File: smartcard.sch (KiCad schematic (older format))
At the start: 9 parts, among them J2101 Smart_Card, U2101 SEC1110

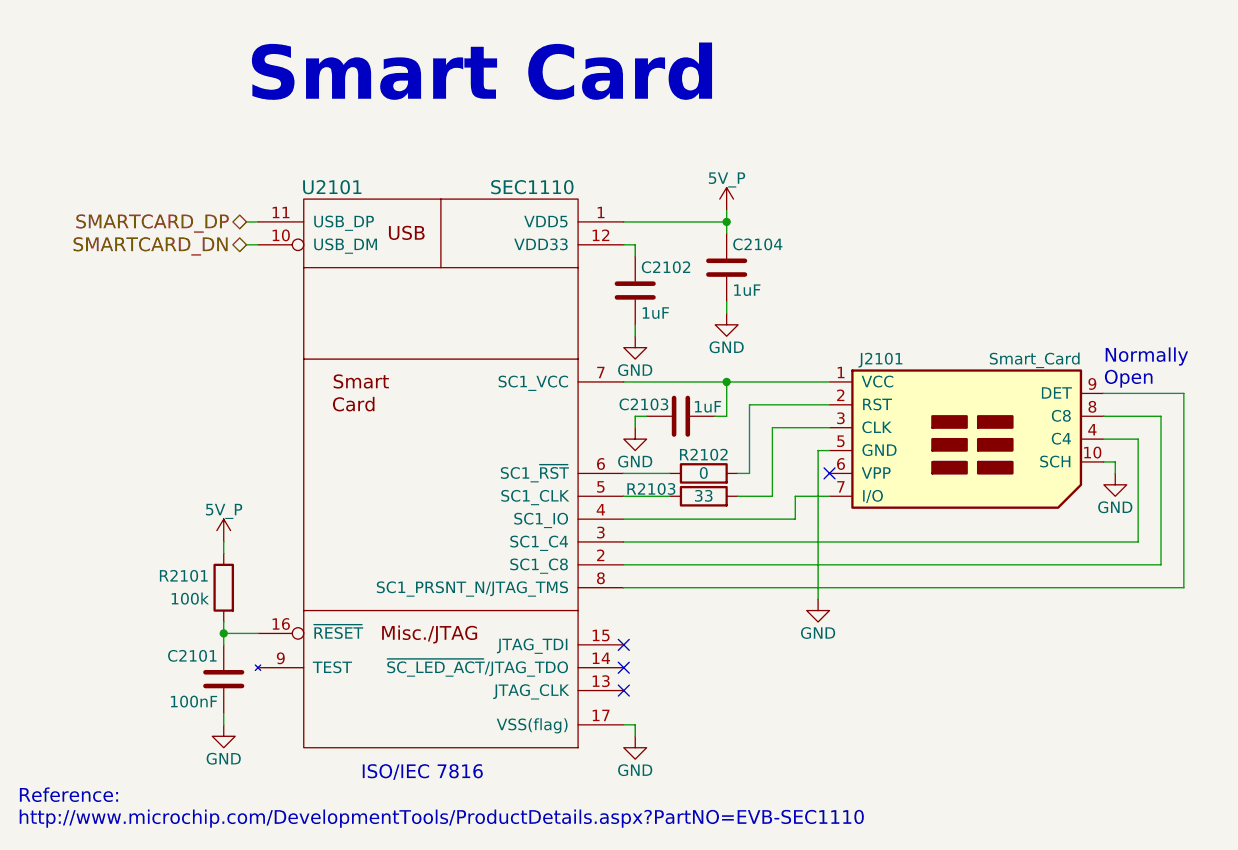
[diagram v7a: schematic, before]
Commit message: Move the WLAN+BT M.2 sheet back to page 18 rather than the last page (24)
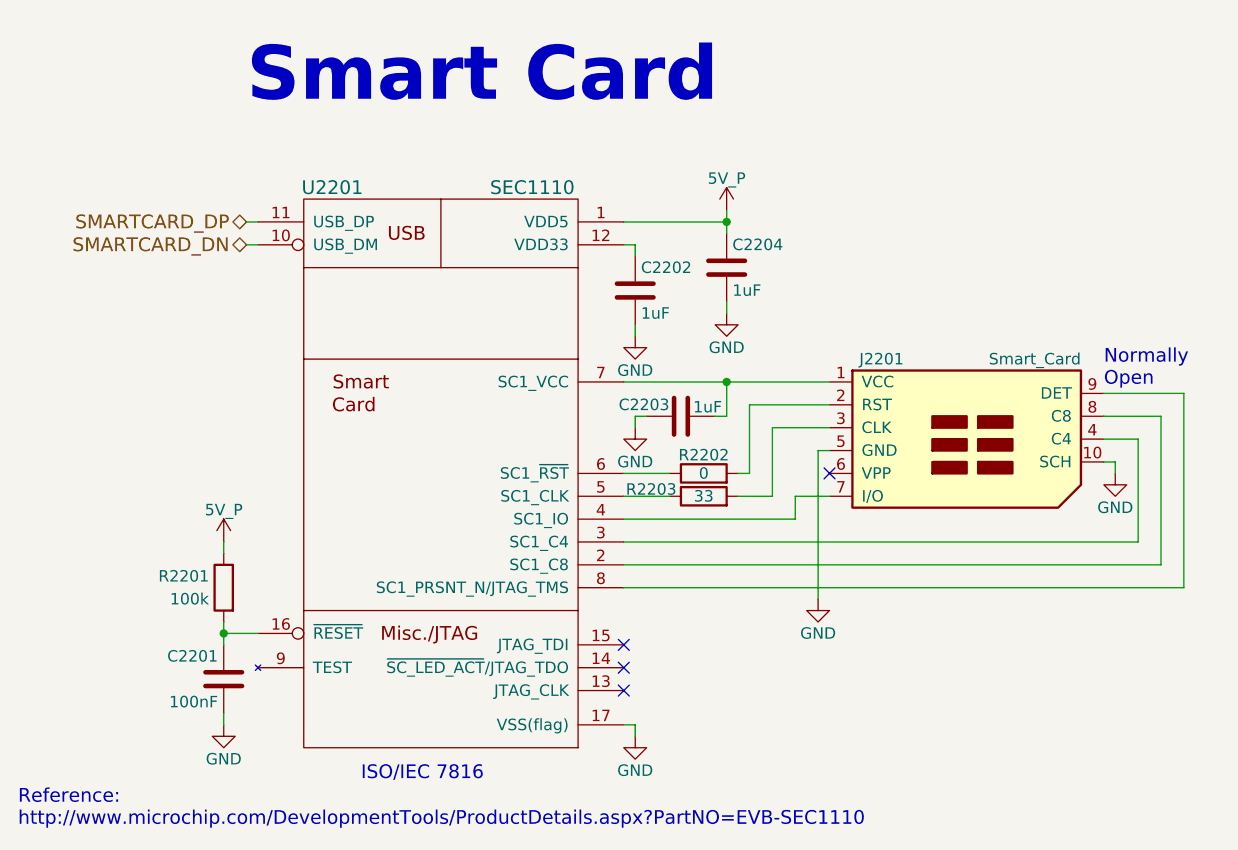
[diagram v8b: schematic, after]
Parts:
- renumbered C2101 to C2201, C2102 to C2202, C2103 to C2203, C2104 to C2204, J2101 to J2201, R2101 to R2201, R2102 to R2202, R2103 to R2203, U2101 to U2201
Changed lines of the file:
@@
 $Descr A4 11693 8268
 encoding utf-8
-Sheet 21 24
+Sheet 22 24
 Title "Smart Card"
-Date "2018-06-14"
+Date "2018-06-15"
 Rev "v0.1.0"
 Comp "Copyright 2018 GNU GPLv3"
@@
 SMARTCARD_DN
 $Comp
-L 5V_P #PWR0333
+L 5V_P #PWR0359
 U 1 1 5B1F0A54
 P 6900 2250
-F 0 "#PWR0333" H 6900 2100 50  0001 C CNN
+F 0 "#PWR0359" H 6900 2100 50  0001 C CNN
 F 1 "5V_P" H 6900 2390 50  0000 C CNN
 F 2 "" H 6900 2250 50  0001 C CNN
@@
 $EndComp
 $Comp
-L C C2102
+L C C2202
 U 1 1 5B1F1971
 P 6500 2600
-F 0 "C2102" H 6525 2700 50  0000 L CNN
+F 0 "C2202" H 6525 2700 50  0000 L CNN
 F 1 "1uF" H 6525 2500 50  0000 L CNN
 F 2 "Capacitors_SMD:C_0603" H 6538 2450 50  0001 C CNN
@@
 $EndComp
 $Comp
-L GND #PWR0334
+L GND #PWR0360
 U 1 1 5B1F199A
 P 6500 2800
-F 0 "#PWR0334" H 6500 2550 50  0001 C CNN
+F 0 "#PWR0360" H 6500 2550 50  0001 C CNN
 F 1 "GND" H 6500 2650 50  0000 C CNN
 F 2 "" H 6500 2800 50  0001 C CNN
@@
 $EndComp
 $Comp
-L C C2104
+L C C2204
 U 1 1 5B1F1CFA
 P 6900 2500
-F 0 "C2104" H 6925 2600 50  0000 L CNN
+F 0 "C2204" H 6925 2600 50  0000 L CNN
 F 1 "1uF" H 6925 2400 50  0000 L CNN
 F 2 "Capacitors_SMD:C_0603" H 6938 2350 50  0001 C CNN
@@
 $EndComp
 $Comp
-L GND #PWR0335
+L GND #PWR0361
 U 1 1 5B1F1D4E
 P 6900 2700
-F 0 "#PWR0335" H 6900 2450 50  0001 C CNN
+F 0 "#PWR0361" H 6900 2450 50  0001 C CNN
 F 1 "GND" H 6900 2550 50  0000 C CNN
 F 2 "" H 6900 2700 50  0001 C CNN
@@
 $EndComp
 $Comp
-L R R2102
+L R R2202
 U 1 1 5B1F2A2C
 P 6800 3400
-F 0 "R2102" V 6880 3400 50  0000 C CNN
+F 0 "R2202" V 6880 3400 50  0000 C CNN
 F 1 "0" V 6800 3400 50  0000 C CNN
 F 2 "Resistors_SMD:R_0603" V 6730 3400 50  0001 C CNN
@@
 $EndComp
 $Comp
-L R R2103
+L R R2203
 U 1 1 5B1F2AD0
 P 6800 3500
-F 0 "R2103" V 6830 3730 50  0000 C CNN
+F 0 "R2203" V 6830 3730 50  0000 C CNN
 F 1 "33" V 6800 3500 50  0000 C CNN
 F 2 "Resistors_SMD:R_0603" V 6730 3500 50  0001 C CNN
@@
 NoConn ~ 6450 4350
 $Comp
-L R R2101
+L R R2201
 U 1 1 5B20FE9D
 P 4700 3900
-F 0 "R2101" H 4875 3950 50  0000 C CNN
+F 0 "R2201" H 4875 3950 50  0000 C CNN
 F 1 "100k" H 4850 3850 50  0000 C CNN
 F 2 "Resistors_SMD:R_0603" V 4630 3900 50  0001 C CNN
@@
 $EndComp
 $Comp
-L 5V_P #PWR0336
+L 5V_P #PWR0362
 U 1 1 5B20FF3B
 P 4700 3700
-F 0 "#PWR0336" H 4700 3550 50  0001 C CNN
+F 0 "#PWR0362" H 4700 3550 50  0001 C CNN
 F 1 "5V_P" H 4700 3840 50  0000 C CNN
 F 2 "" H 4700 3700 50  0001 C CNN
@@
 $EndComp
 $Comp
-L C C2101
+L C C2201
 U 1 1 5B20FF65
 P 4700 4300
-F 0 "C2101" H 4725 4400 50  0000 L CNN
+F 0 "C2201" H 4725 4400 50  0000 L CNN
 F 1 "100nF" H 4725 4200 50  0000 L CNN
 F 2 "Capacitors_SMD:C_0603" H 4738 4150 50  0001 C CNN
@@
 $EndComp
 $Comp
-L GND #PWR0337
+L GND #PWR0363
 U 1 1 5B20FFAF
 P 4700 4500
-F 0 "#PWR0337" H 4700 4250 50  0001 C CNN
+F 0 "#PWR0363" H 4700 4250 50  0001 C CNN
 F 1 "GND" H 4700 4350 50  0000 C CNN
 F 2 "" H 4700 4500 50  0001 C CNN
@@
 $EndComp
 $Comp
-L C C2103
+L C C2203
 U 1 1 5B210DE6
 P 6700 3150
-F 0 "C2103" V 6750 3200 50  0000 L CNN
+F 0 "C2203" V 6750 3200 50  0000 L CNN
 F 1 "1uF" V 6740 2970 50  0000 L CNN
 F 2 "Capacitors_SMD:C_0603" H 6738 3000 50  0001 C CNN
@@
 $EndComp
 $Comp
-L GND #PWR0338
+L GND #PWR0364
 U 1 1 5B210E33
 P 6500 3200
-F 0 "#PWR0338" H 6500 2950 50  0001 C CNN
+F 0 "#PWR0364" H 6500 2950 50  0001 C CNN
 F 1 "GND" H 6500 3050 50  0000 C CNN
 F 2 "" H 6500 3200 50  0001 C CNN
@@
 $EndComp
 $Comp
-L GND #PWR0339
+L GND #PWR0365
 U 1 1 5B21589D
 P 6500 4550
-F 0 "#PWR0339" H 6500 4300 50  0001 C CNN
+F 0 "#PWR0365" H 6500 4300 50  0001 C CNN
 F 1 "GND" H 6500 4400 50  0000 C CNN
 F 2 "" H 6500 4550 50  0001 C CNN
@@
 ISO/IEC 7816
 $Comp
-L SEC1110 U2101
+L SEC1110 U2201
 U 1 1 5B265531
 P 5650 3400
-F 0 "U2101" H 5175 4650 60  0000 C CNN
+F 0 "U2201" H 5175 4650 60  0000 C CNN
 F 1 "SEC1110" H 6050 4650 60  0000 C CNN
 F 2 "" H 5650 3700 60  0001 C CNN
@@
 $EndComp
 $Comp
-L SMART_CARD J2101
+L SMART_CARD J2201
 U 1 1 5B26711A
 P 7850 3300
-F 0 "J2101" H 7675 3700 50  0000 R CNN
+F 0 "J2201" H 7675 3700 50  0000 R CNN
 F 1 "Smart_Card" H 8450 3700 50  0000 R CNN
 F 2 "dvk-mx8m-bsb:Conn_Amphenol_SIMcard_10100271" H 7850 3650 50  0001 C CNN
@@
 NoConn ~ 7350 3400
 $Comp
-L GND #PWR0340
+L GND #PWR0366
 U 1 1 5B27C54B
 P 7300 3950
-F 0 "#PWR0340" H 7300 3700 50  0001 C CNN
+F 0 "#PWR0366" H 7300 3700 50  0001 C CNN
 F 1 "GND" H 7300 3800 50  0000 C CNN
 F 2 "" H 7300 3950 50  0001 C CNN
@@
 Normally\nOpen
 $Comp
-L GND #PWR0341
+L GND #PWR0367
 U 1 1 5B296537
 P 8600 3400
-F 0 "#PWR0341" H 8600 3150 50  0001 C CNN
+F 0 "#PWR0367" H 8600 3150 50  0001 C CNN
 F 1 "GND" H 8600 3250 50  0000 C CNN
 F 2 "" H 8600 3400 50  0001 C CNN
